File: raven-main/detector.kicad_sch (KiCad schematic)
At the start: 7 parts, among them U8 OPA656UB, U9 TLV3201AIDCKT

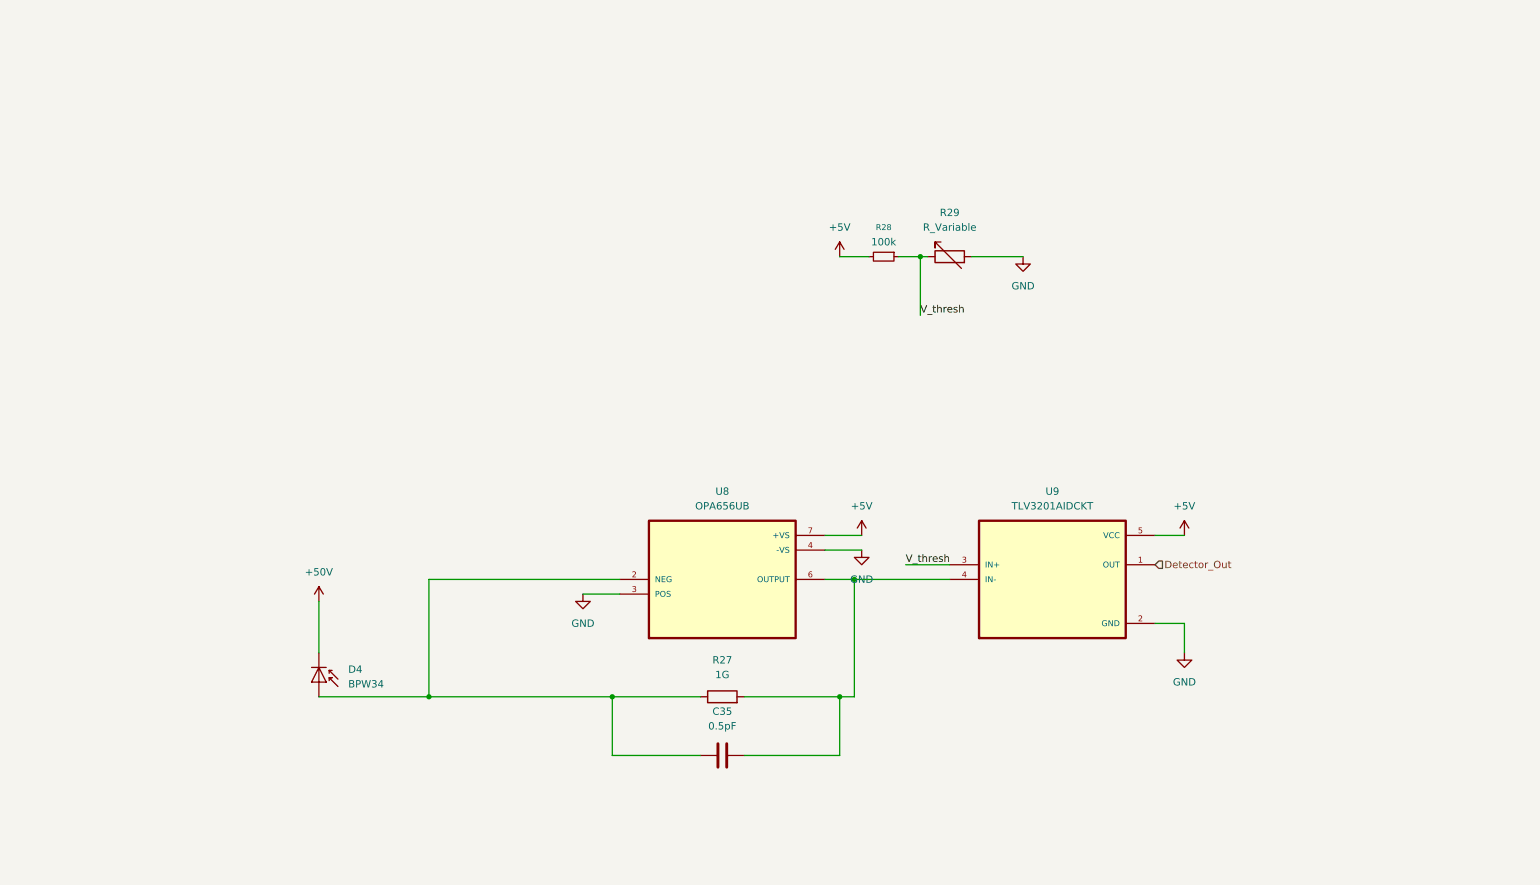
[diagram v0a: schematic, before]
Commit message: Swap detector amp to ADA4817, add bias filters and hysteresis
Detector front-end revisions from bench-planning session:

- Replace obsolete OPA656 with ADA4817-1 (JFET, 5V single-supply,
  CMR to negative rail - resolves 0V common-mode issue)
- Add ADA4817 footprint/symbol library files
- Add per-diode RC bias filter on 50V rail (R30/C39, R32/C40)
  to reject boost-converter ripple
- Add comparator hysteresis network (R31/R34) plus threshold
  floor resistor (R37) to prevent chatter and stop threshold
  collapsing to zero
- Add 10uF bulk decoupling alongside 100nF on amp supply
- Duplicate channel A to channel B (independent two-channel)

Open: confirm comparator edge polarity on bench before firmware;
run ERC (check PWR_FLAG on 50V/5V nets).
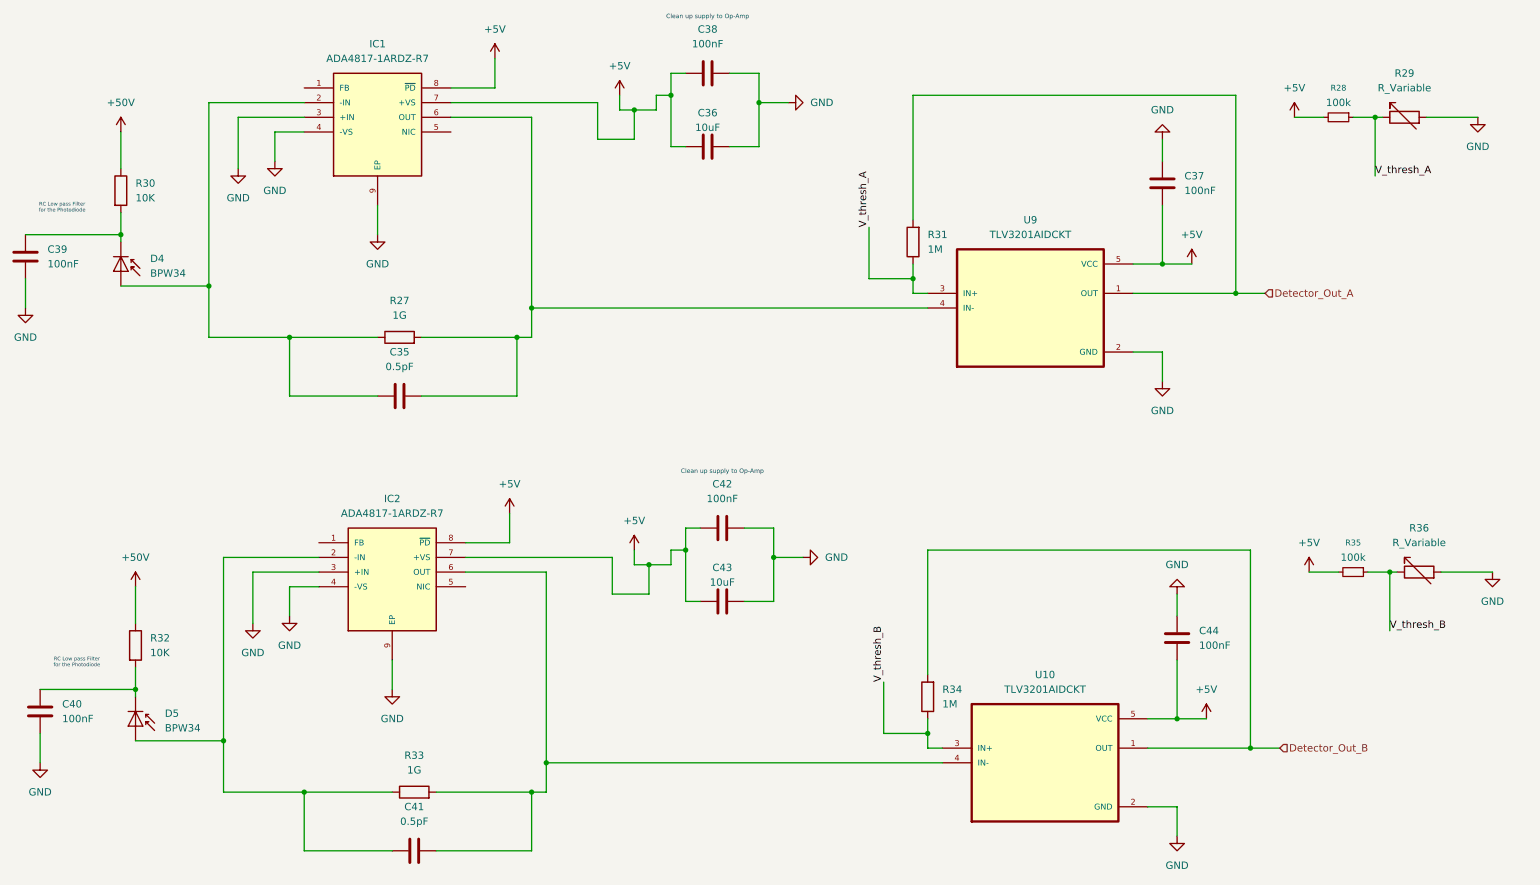
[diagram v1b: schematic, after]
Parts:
- removed U8: OPA656UB, OPA656UB:SOIC127P599X175-8N, symbol OPA656UB:OPA656UB
- added C36, C43: 10uF, symbol Device:C
- added C37, C38, C39, C40, C42, C44: 100nF, symbol Device:C
- added C41: 0.5pF, Capacitor_SMD:C_0402_1005Metric, symbol Device:C
- added D5: BPW34, OptoDevice:Osram_DIL2_4.3x4.65mm_P5.08mm, symbol Sensor_Optical:BPW34
- added IC1, IC2: ADA4817-1ARDZ-R7, ADA4817-1ARDZ-R7:SOIC127P600X175-9N, symbol ADA4817-1ARDZ-R7:ADA4817-1ARDZ-R7
- added R30, R32: 10K, symbol Device:R
- added R31, R34: 1M, symbol Device:R
- added R33: 1G, Resistor_SMD:R_0402_1005Metric, symbol Device:R
- added R35: 100k, Resistor_SMD:R_0402_1005Metric, symbol Device:R_Small
- added R36: R_Variable, Resistor_SMD:R_0402_1005Metric, symbol Device:R_Variable
- added U10: TLV3201AIDCKT, TLV3201AIDCKT:SOT65P210X110-5N, symbol TLV3201AIDCKT:TLV3201AIDCKT
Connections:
- net +50V: now also R30.1, R32.1; no longer D4.1 (K)
- net +5V: now also C36.1, C37.2, C38.2, C42.2, C43.1, C44.2, IC1.7 (+VS), IC1.8 (~{PD}), IC2.7 (+VS), IC2.8 (~{PD}), R35.2, U10.5 (VCC)
- net GND: now also C36.2, C37.1, C38.1, C39.2, C40.2, C42.1, C43.2, C44.1, IC1.3 (+IN), IC1.4 (-VS), IC1.9 (EP), IC2.3 (+IN), IC2.4 (-VS), IC2.9 (EP), R36.2, U10.2 (GND)
- net at C35.1, D4.2 (A), R27.1: now also IC1.2 (-IN)
- net at C35.2, R27.2, U9.4 (IN-): now also IC1.6 (OUT)
- net Detector_Out renamed Detector_Out_A
- net Detector_Out_A: now also R31.2
- net V_thresh renamed V_thresh_A
- net V_thresh_A: now also R31.1
- new net: C39.1, D4.1 (K), R30.2
- new net: C41.1, D5.2 (A), IC2.2 (-IN), R33.1
- new net: C41.2, IC2.6 (OUT), R33.2, U10.4 (IN-)
- new net: C40.1, D5.1 (K), R32.2
- new net Detector_Out_B: R34.2, U10.1 (OUT)
- new net V_thresh_B: R34.1, R35.1, R36.1, U10.3 (IN+)
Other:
- note added: "Clean up supply to Op-Amp"
- note added: "RC Low pass Filter for the Photodiode"
- moved on the sheet: C35, D4, R27, R28, R29, U9

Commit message: Add Detector-Proto-Board: complete layout ready for fab
Standalone single-channel proto board (D4/R27/C35/IC1 charge amp +
U9 comparator) extracted from the main RAVEN board, for bench-testing
the amplifier design before committing it to the full board.

Includes:
- Full schematic + routed PCB layout (40x30mm, 2-layer)
- GND poured on both F.Cu and B.Cu, stitched with vias
- R37/R32 floor resistor added to threshold divider (200R)
- R31 corrected to 200k (was 1M) per hysteresis recalculation
- Added TVS/ESD protection at J1 (D1: SMAJ58A on +50V, D2: SMAJ5.0A
  on +5V, D3: PESD5V0S1BA on Detector_Out_A)
- DRC clean: 0 violations, 0 unconnected items

Open items for bench testing:
- Confirm comparator edge polarity (rising vs falling) before
  writing ESP32 interrupt firmware
- Verify hysteresis band matches ~5-25mV calculated range
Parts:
- added R37: 200, Resistor_SMD:R_0402_1005Metric, symbol Device:R_Small
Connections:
- net GND: now also R37.1; no longer R29.2
- new net: R29.2, R37.2
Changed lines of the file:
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@@
+	(wire
+		(pts
+			(xy 273.05 31.75) (xy 278.13 31.75)
+		)
+		(stroke
+			(width 0)
+			(type default)
+		)
+	)
 	(wire
 		(pts
@@
 	(wire
 		(pts
-			(xy 262.89 31.75) (xy 271.78 31.75)
-		)
-		(stroke
-			(width 0)
-			(type default)
-		)
-	)
-	(wire
-		(pts
 			(xy 176.53 140.97) (xy 179.07 140.97)
 		)
@@
 		(pts
 			(xy 88.9 80.01) (xy 105.41 80.01)
+		)
+		(stroke
+			(width 0)
+			(type default)
+		)
+	)
+	(wire
+		(pts
+			(xy 262.89 31.75) (xy 267.97 31.75)
 		)
 		(stroke
@@
 	(symbol
 		(lib_id "power:GND")
-		(at 271.78 31.75 0)
+		(at 278.13 31.75 0)
 		(unit 1)
 		(body_style 1)
@@
 		(fields_autoplaced yes)
 		(property "Reference" "#PWR061"
-			(at 271.78 38.1 0)
+			(at 278.13 38.1 0)
 			(hide yes)
 			(show_name no)
@@
 		)
 		(property "Value" "GND"
-			(at 271.78 36.83 0)
+			(at 278.13 36.83 0)
 			(show_name no)
 			(do_not_autoplace no)
@@
 		)
 		(property "Footprint" ""
-			(at 271.78 31.75 0)
+			(at 278.13 31.75 0)
 			(hide yes)
 			(show_name no)
@@
 		)
 		(property "Datasheet" ""
-			(at 271.78 31.75 0)
+			(at 278.13 31.75 0)
 			(hide yes)
 			(show_name no)
@@
 		)
 		(property "Description" "Power symbol creates a global label with name \"GND\" , ground"
-			(at 271.78 31.75 0)
+			(at 278.13 31.75 0)
 			(hide yes)
 			(show_name no)
@@
 					(unit 1)
 				)
+			)
+		)
+	)
+	(symbol
+		(lib_id "Device:R_Small")
+		(at 270.51 31.75 270)
+		(unit 1)
+		(body_style 1)
+		(exclude_from_sim no)
+		(in_bom yes)
+		(on_board yes)
+		(in_pos_files yes)
+		(dnp no)
+		(fields_autoplaced yes)
+		(property "Reference" "R37"
+			(at 270.51 26.67 90)
+			(show_name no)
+			(do_not_autoplace no)
+			(effects
+				(font
+					(size 1.016 1.016)
+				)
+			)
+		)
+		(property "Value" "200"
+			(at 270.51 29.21 90)
+			(show_name no)
+			(do_not_autoplace no)
+			(effects
+				(font
+					(size 1.27 1.27)
+				)
+			)
+		)
+		(property "Footprint" "Resistor_SMD:R_0402_1005Metric"
+			(at 270.51 31.75 0)
+			(hide yes)
+			(show_name no)
+			(do_not_autoplace no)
+			(effects
+				(font
+					(size 1.27 1.27)
+				)
+			)
+		)
+		(property "Datasheet" ""
+			(at 270.51 31.75 0)
+			(hide yes)
+			(show_name no)
+			(do_not_autoplace no)
+			(effects
+				(font
+					(size 1.27 1.27)
+				)
+			)
+		)
+		(property "Description" "Resistor, small symbol"
+			(at 270.51 31.75 0)
+			(hide yes)
+			(show_name no)
+			(do_not_autoplace no)
+			(effects
+				(font
+					(size 1.27 1.27)
+				)
+			)
+		)
+		(pin "1"
+		)
+		(pin "2"
+		)
+		(instances
+			(project "raven-main"
+				(path "/c13cbf2f-9bb3-45e9-94dd-cb1d58494ac8/8ed86ece-68a5-4e2a-83b7-03315ba32bdd"
+					(reference "R37")
+					(unit 1)
+				)
